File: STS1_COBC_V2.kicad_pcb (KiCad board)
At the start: 4 copper layers, 81 x 85 mm, 197 parts, among them IC2 STWD100PYW83F, IC3 STM32F411RET6TR, J1 UHF, J12 Conn_01x01_Male, J13 Conn_01x01_Male, J16 Conn_ARM_JTAG_SWD_10, J17 Conn_01x03_Male, J3 Conn_01x01_Male, J4 Conn_01x01_Male, J5 Conn_01x03_Male, J6 Conn_01x01_Male, J7 Conn_01x01_Male, J8 Conn_01x01_Male, J9 Conn_01x01_Male, Q1 SQ2318, Q2 BSS123, U1 coordinate_system, U10 TQP3M9036, U11 QPC1022, U12 FPF2701, U13 TQP7M9106, U2 LP2985-1.8, U3 MCP1725-3302E_MC, U4 74LVC2G74, U5 TYKTBCSANF-26.000000, U7 NL17SV04XV5T2G, U8 Si4463, U9 LFCG-490+, Y1 Crystal_GND24

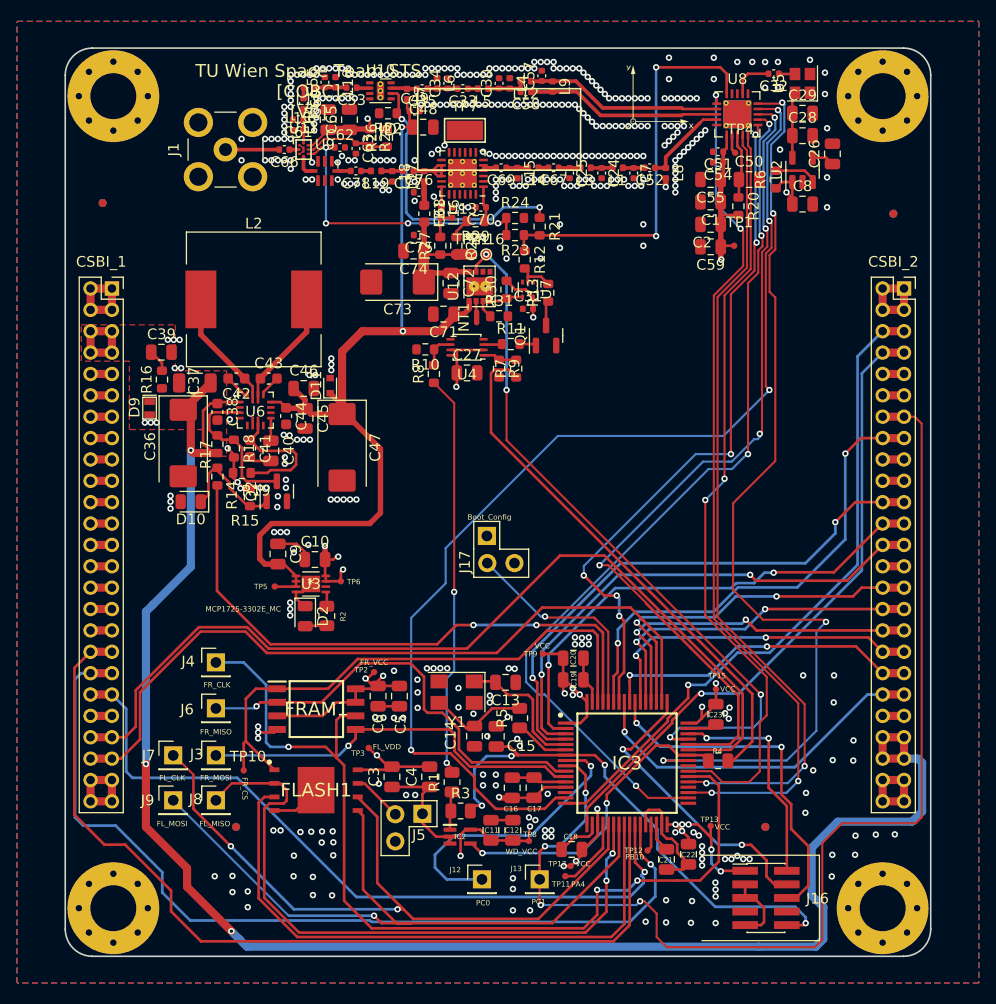
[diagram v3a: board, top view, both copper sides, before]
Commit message: Remove old submodules
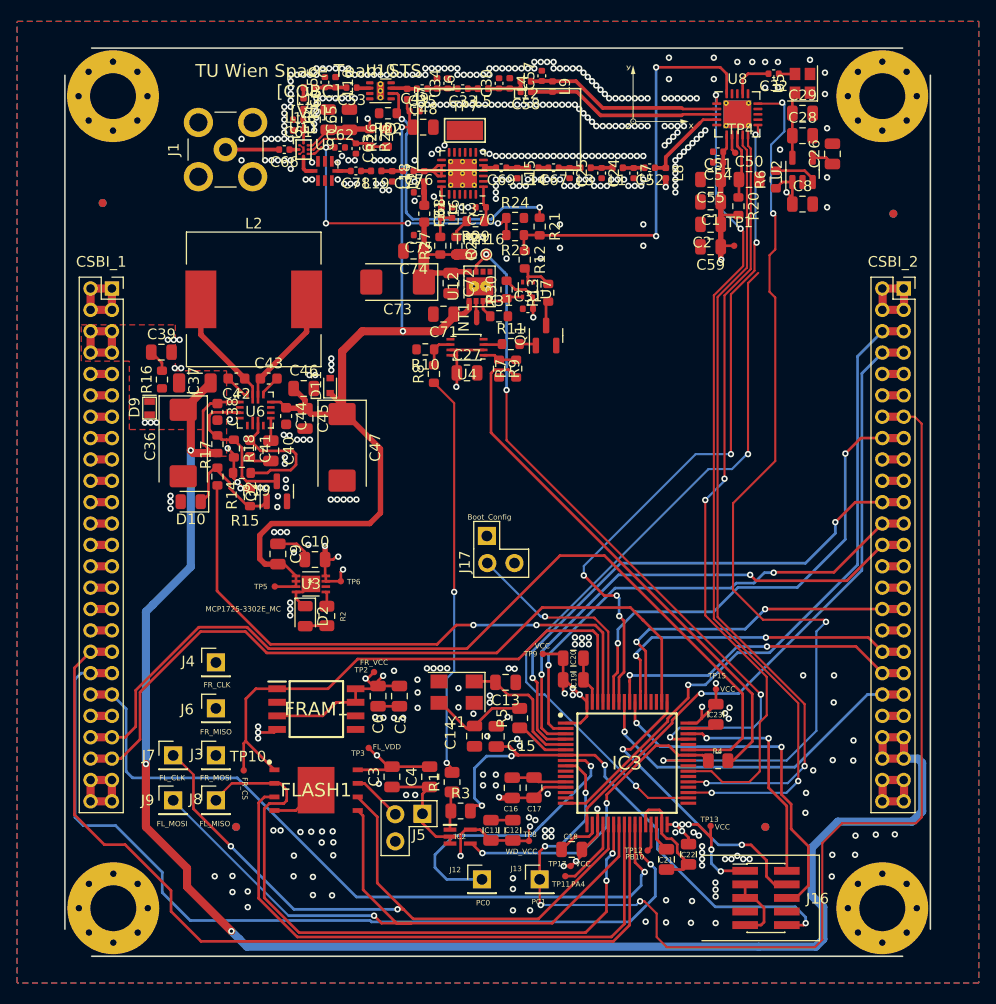
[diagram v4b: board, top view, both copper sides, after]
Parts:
- C52: value C -> 8.2p
- C57: value C -> 3.9p
- C58: value C -> 2.2p
- L12: value L -> 51n
- L8: value L -> 220n
- L9: value L -> 56n
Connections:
- FRAM1 pad 2: /SPI_FRAM_MISO -> /STS1_connector/COBC_SPI_3
- FRAM1 pad 5: /SPI_FRAM_MOSI -> /STS1_connector/COBC_SPI_2
- FRAM1 pad 6: /SPI_FRAM_CLK -> /STS1_connector/COBC_SPI_1
- IC3 pad 10: /SPI_FRAM_MISO -> /Si4463_SDO
- IC3 pad 11: /SPI_FRAM_MOSI -> /Si4463_SDI
- IC3 pad 15: /Si4463_SDI -> unconnected-(IC3-Pad15)
- IC3 pad 34: /Si4463_CLK -> unconnected-(IC3-Pad34)
- IC3 pad 38: /SPI_FRAM_CLK -> /Si4463_CLK
- IC3 pad 44: /Si4463_SDO -> unconnected-(IC3-Pad44)
- J3 pad 1: /SPI_FRAM_MOSI -> /Si4463_SDI
- J4 pad 1: /SPI_FRAM_CLK -> /Si4463_CLK
- J6 pad 1: /SPI_FRAM_MISO -> /Si4463_SDO
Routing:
- net /Si4463_SDI: track 103.7 -> 0.00 mm, vias 4 -> 0
- net /SPI_FRAM_CLK: track 87.7 -> 0.00 mm, vias 3 -> 0
- net /Si4463_CLK: track 84.1 -> 0.00 mm, vias 4 -> 0
- net /Si4463_SDO: track 79.3 -> 0.00 mm, vias 4 -> 0
- net unconnected-(IC3-Pad34): track 0.00 -> 68.3 mm, vias 0 -> 2
- net /SPI_FRAM_MISO: track 41.6 -> 0.00 mm, vias 1 -> 0
- net /SPI_FRAM_MOSI: track 37.0 -> 0.00 mm, vias 1 -> 0
- net /STS1_connector/COBC_SPI_1: track 34.5 -> 2.00 mm, vias 2 -> 0
- net /STS1_connector/COBC_SPI_3: track 33.0 -> 2.00 mm, vias 2 -> 0
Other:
- outline, holes or cut-outs redrawn

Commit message: V2.5
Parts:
- removed D10: BZY55C12 RYG, Diode_SMD:D_0805_2012Metric
- removed D11: AQ1003-01LTG, Diode_SMD:D_SOD-523
- removed D9: UCLAMP0871P.TNT, STS_Package_DFN_QFN:SGP1610N2
- added D1: UCLAMP0871P.TNT, STS_Package_DFN_QFN:SGP1610N2, F.Cu at (123.6, 73.0)
- added D3: BZY55C12 RYG, Diode_SMD:D_0805_2012Metric, F.Cu at (128.0, 83.6)
- added D4: AQ1003-01LTG, Diode_SMD:D_SOD-523, F.Cu at (142.3, 76.2)
- added D5: LED, LED_SMD:LED_0805_2012Metric, F.Cu at (150.0, 87.9)
- added D6: LED, LED_SMD:LED_0805_2012Metric, F.Cu at (150.0, 90.0)
- added D7: LED, LED_SMD:LED_0805_2012Metric, F.Cu at (187.9, 112.3)
- added D8: LED, LED_SMD:LED_0805_2012Metric, F.Cu at (187.9, 110.2)
- added JP1: SolderJumper_2_Open, Jumper:SolderJumper-2_P1.3mm_Open_TrianglePad1.0x1.5mm, F.Cu at (174.8, 121.3)
- added R32: 220R, Resistor_SMD:R_0805_2012Metric, F.Cu at (146.4, 87.9)
- added R33: 220R, Resistor_SMD:R_0805_2012Metric, F.Cu at (146.4, 90.0)
- added R34: 220R, Resistor_SMD:R_0805_2012Metric, F.Cu at (180.2, 112.9)
- added R35: 220R, Resistor_SMD:R_0805_2012Metric, F.Cu at (180.2, 110.9)
- added TP14: TestPoint, STS1library:STS1_Testpoint, F.Cu at (184.9, 98.5)
- J16: footprint STS1library:PinHeader_2x05_P1.27mm_Vertical_SMD -> STS_connector:SAMTEC_FTSH-105-01-X-DH-A
- U1: footprint STS:Coordinates -> STS_connector:Coordinates
- U6: value ~ -> MP28167GQ
- moved J6 73.4 mm to (188.9, 59.5)
- moved J3 73.3 mm to (185.2, 59.5)
- moved J4 65.8 mm to (185.2, 63.2)
- moved U1 49.8 mm to (122.8, 55.4)
- moved FRAM1 46.0 mm to (185.6, 102.2)
- moved C6 42.5 mm to (187.7, 106.2), turned to 180 degrees
- moved TP2 42.4 mm to (186.7, 107.9)
- moved C5 41.2 mm to (188.4, 98.2), turned to 0 degrees
- moved C36 13.8 mm to (125.3, 65.1), turned to 90 degrees
- moved FID1 12.9 mm to (173.4, 124.6)
- moved FID8 12.9 mm to (173.4, 124.6)
- moved C47 8.42 mm to (150.4, 78.5)
- moved C39 7.34 mm to (126.1, 77.5), turned to 180 degrees
- moved R14 5.34 mm to (128.5, 86.9)
- moved C40 5.18 mm to (136.4, 74.4), turned to 0 degrees
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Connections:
- FLASH1 pad 1: /SPI_FRAM_CS -> /SPI_FLASH_CS
- IC3 pad 33: unconnected-(IC3-Pad33) -> Net-(IC3-Pad33)
- IC3 pad 34: unconnected-(IC3-Pad34) -> /SPI_FRAM_CS
- IC3 pad 36: unconnected-(IC3-Pad36) -> Net-(IC3-Pad36)
- IC3 pad 62: /SPI_FRAM_CS -> /SPI_FLASH_CS
- J16 pad 1: +3V3 -> Net-(J16-Pad1)
- TP10 pad 1: /SPI_FRAM_CS -> /SPI_FLASH_CS
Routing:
- net /Si4463_SDO: track 0.00 -> 95.6 mm, vias 0 -> 2
- net /Si4463_SDI: track 0.00 -> 92.0 mm, vias 0 -> 2
- net /Si4463_CLK: track 0.00 -> 71.8 mm, vias 0 -> 2
- net unconnected-(IC3-Pad34): track 68.3 -> 0.00 mm, vias 2 -> 0
- net AGND: track 119.5 -> 167.6 mm, vias 417 -> 490
- net /STS1_connector/COBC_SPI_1: track 2.00 -> 49.8 mm, vias 0 -> 3
- net /SPI_FLASH_CS: track 0.00 -> 43.7 mm
- net /STS1_connector/COBC_SPI_3: track 2.00 -> 39.0 mm, vias 0 -> 2
- net /SPI_FRAM_CS: track 52.5 -> 23.0 mm, vias 0 -> 2
- net /STS1_connector/COBC_SPI_2: track 32.3 -> 43.8 mm, vias 2 -> 3
- net Net-(C42-Pad1): track 11.2 -> 0.00 mm
- net Net-(C43-Pad1): track 11.1 -> 0.00 mm
- net +5V: track 87.5 -> 77.3 mm
- net Net-(C41-Pad1): track 12.3 -> 3.51 mm
- net /COBC STM/SWDIO: track 20.8 -> 27.9 mm
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- added copper zone on F.Cu, net +3V3
- added copper zone on F.Cu, net +5V
- added copper zone on In2.Cu, net AGND
- added copper zone on F.Cu, net Net-(C42-Pad1)
- added copper zone on F.Cu, net Net-(C43-Pad1)
- added copper zone on B.Cu, net VBUS
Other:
- outline, holes or cut-outs redrawn
- rule pad_to_mask_clearance: 0.19 -> 0
- board text added: "3V3"
- board text added: "5V"
- board text added: "FRAM_CS"
- board text added: "F_CS"
- board text added: "PB12"
- board text added: "PB15"
- board text added: "RF_CLK"
- board text added: "RF_SDI"
- board text added: "RF_SDO"
- board text added: "TU Wien Space Team STS1 COBC V2.5"
- board text removed: "FR_CLK"
- board text removed: "FR_CS"
- board text removed: "FR_MISO"
- board text removed: "FR_MOSI"
- board text removed: "PB10"
- board text removed: "TU Wien Space Team STS [COBC] [V2]"
